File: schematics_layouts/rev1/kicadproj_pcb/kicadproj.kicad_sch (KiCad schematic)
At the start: 16 parts, among them J1 DS3231_board, J2 LM386_board, J3 microSD_board, Q1 Si2323DS_on_TO220, Q2 Si2323DS_on_TO220, SW1 WAKE Switch, SW2 SET 15MIN, U2 ATmega328P-PU

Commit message: Updated PCB layout
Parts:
- BT1, C2, C4: footprint (none) -> Connector_PinHeader_2.54mm:PinHeader_1x02_P2.54mm_Vertical
- C1, C3, C5, Q1, Q2, SW1, SW2: footprint (none) -> Connector_PinHeader_2.54mm:PinHeader_1x03_P2.54mm_Vertical
- J1, J3: footprint (none) -> Connector_PinHeader_2.54mm:PinHeader_1x06_P2.54mm_Vertical
- J2, R1, R2: footprint (none) -> Connector_PinHeader_2.54mm:PinHeader_1x04_P2.54mm_Vertical
- U2: footprint (none) -> Package_DIP:DIP-28_W7.62mm
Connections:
- net GND: now also C1.3, C3.3, C5.3, SW1.3 (2); no longer C1.2, C3.2, C5.2, SW1.2
- net at U2.1 (Pin_1): now also R1.4; no longer R1.2
- new net: R2.4, SW2.3 (2), U2.5 (Pin_5)
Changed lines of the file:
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@@
 			)
 		)
-		(property "Footprint" ""
+		(property "Footprint" "Connector_PinHeader_2.54mm:PinHeader_1x04_P2.54mm_Vertical"
 			(at 176.53 85.09 0)
 			(effects
@@
 			)
 		)
-		(property "Footprint" ""
+		(property "Footprint" "Package_DIP:DIP-28_W7.62mm"
 			(at 133.35 86.36 0)
 			(effects
@@
 	)
 	(symbol
+		(lib_name "R_1")
 		(lib_id "Device:R")
 		(at 119.38 71.12 90)
@@
 			)
 		)
-		(property "Footprint" ""
+		(property "Footprint" "Connector_PinHeader_2.54mm:PinHeader_1x04_P2.54mm_Vertical"
 			(at 119.38 72.898 90)
 			(effects
@@
 		(pin "1"
 		)
-		(pin "2"
+		(pin "4"
 		)
 		(instances
@@
 			)
 		)
-		(property "Footprint" ""
+		(property "Footprint" "Connector_PinHeader_2.54mm:PinHeader_1x02_P2.54mm_Vertical"
 			(at 153.3652 99.06 0)
 			(effects
@@
 			)
 		)
-		(property "Footprint" ""
+		(property "Footprint" "Connector_PinHeader_2.54mm:PinHeader_1x03_P2.54mm_Vertical"
 			(at 176.53 49.53 0)
 			(effects
@@
 			)
 		)
-		(property "Footprint" ""
+		(property "Footprint" "Connector_PinHeader_2.54mm:PinHeader_1x03_P2.54mm_Vertical"
 			(at 75.8952 104.14 0)
 			(effects
@@
 		(pin "1"
 		)
-		(pin "2"
+		(pin "3"
 		)
 		(instances
@@
 			)
 		)
-		(property "Footprint" ""
+		(property "Footprint" "Connector_PinHeader_2.54mm:PinHeader_1x06_P2.54mm_Vertical"
 			(at 176.53 67.31 0)
 			(effects
@@
 	)
 	(symbol
+		(lib_name "C_2")
 		(lib_id "Device:C")
 		(at 87.63 74.93 0)
@@
 			)
 		)
-		(property "Footprint" ""
+		(property "Footprint" "Connector_PinHeader_2.54mm:PinHeader_1x03_P2.54mm_Vertical"
 			(at 88.5952 78.74 0)
 			(effects
@@
 		(pin "1"
 		)
-		(pin "2"
+		(pin "3"
 		)
 		(instances
@@
 	)
 	(symbol
+		(lib_name "C_1")
 		(lib_id "Device:C")
 		(at 80.01 74.93 0)
@@
 			)
 		)
-		(property "Footprint" ""
+		(property "Footprint" "Connector_PinHeader_2.54mm:PinHeader_1x02_P2.54mm_Vertical"
 			(at 79.0448 78.74 0)
 			(effects
@@
 			)
 		)
-		(property "Footprint" ""
+		(property "Footprint" "Connector_PinHeader_2.54mm:PinHeader_1x06_P2.54mm_Vertical"
 			(at 176.53 102.87 0)
 			(effects
@@
 			)
 		)
-		(property "Footprint" ""
+		(property "Footprint" "Connector_PinHeader_2.54mm:PinHeader_1x02_P2.54mm_Vertical"
 			(at 113.03 52.07 0)
 			(effects
@@
 			)
 		)
-		(property "Footprint" ""
+		(property "Footprint" "Connector_PinHeader_2.54mm:PinHeader_1x03_P2.54mm_Vertical"
 			(at 113.03 43.18 0)
 			(effects
@@
 			)
 		)
-		(property "Footprint" ""
+		(property "Footprint" "Connector_PinHeader_2.54mm:PinHeader_1x04_P2.54mm_Vertical"
 			(at 105.41 83.058 90)
 			(effects
@@
 		(pin "1"
 		)
-		(pin "2"
+		(pin "4"
 		)
 		(instances
@@
 			)
 		)
-		(property "Footprint" ""
+		(property "Footprint" "Connector_PinHeader_2.54mm:PinHeader_1x03_P2.54mm_Vertical"
 			(at 107.95 90.17 0)
 			(effects
@@
 			)
 		)
-		(pin "2"
+		(pin "3"
 		)
 		(pin "1"
@@
 	)
 	(symbol
+		(lib_name "SW_Push_1")
 		(lib_id "Switch:SW_Push")
 		(at 146.05 40.64 0)
@@
 			)
 		)
-		(property "Footprint" ""
+		(property "Footprint" "Connector_PinHeader_2.54mm:PinHeader_1x03_P2.54mm_Vertical"
 			(at 146.05 35.56 0)
 			(effects
@@
 			)
 		)
-		(pin "2"
+		(pin "3"
 		)
 		(pin "1"
@@
 	)
 	(symbol
+		(lib_name "CP_1")
 		(lib_id "Device:CP")
 		(at 199.39 86.36 0)
@@
 			)
 		)
-		(property "Footprint" ""
+		(property "Footprint" "Connector_PinHeader_2.54mm:PinHeader_1x03_P2.54mm_Vertical"
 			(at 200.3552 90.17 0)
 			(effects
@@
 			)
 		)
-		(pin "2"
-		)
-		(pin "1"
+		(pin "3"
+		)
+		(pin "1"

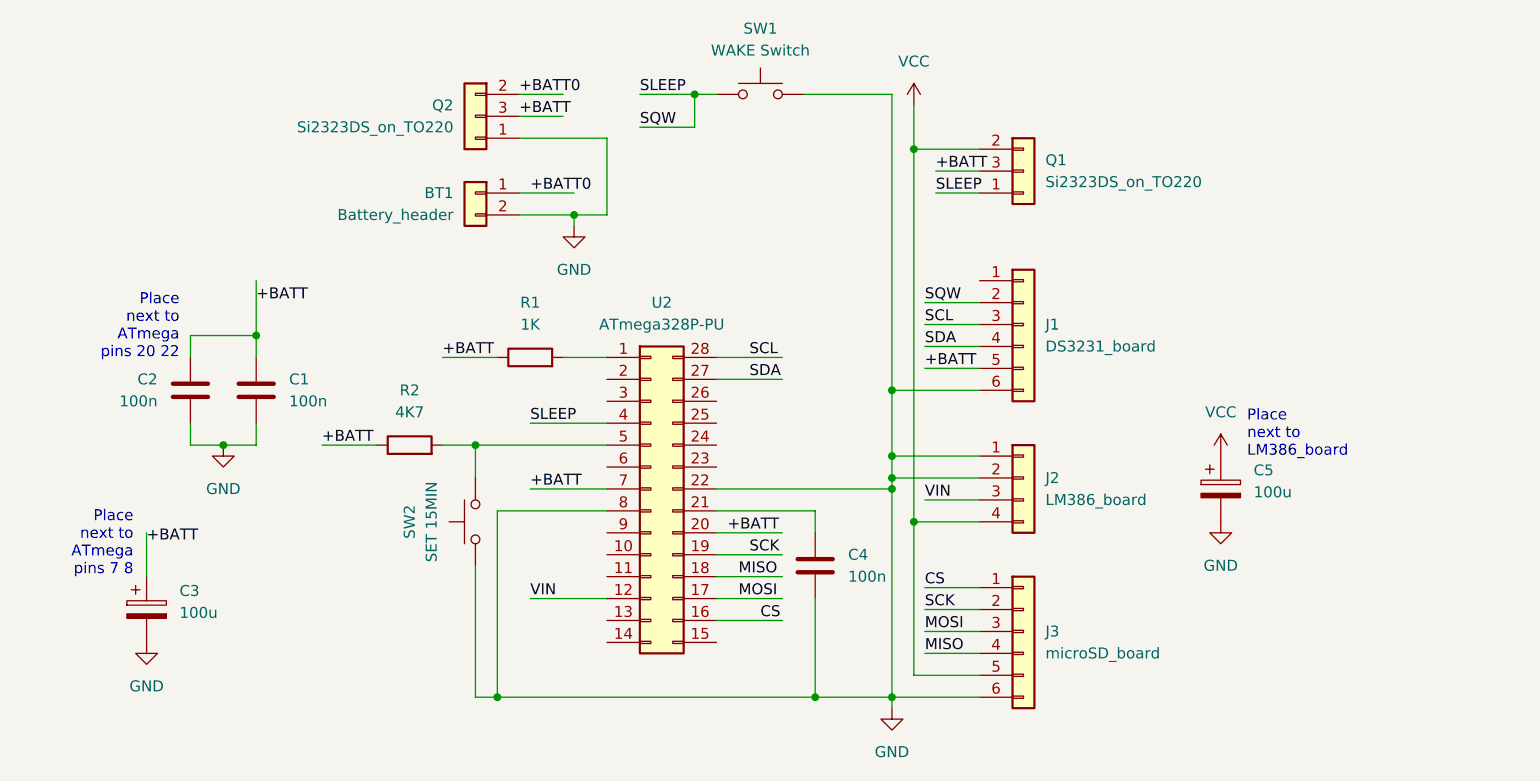
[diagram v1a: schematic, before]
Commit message: Revised PCB layout; Updated documentation
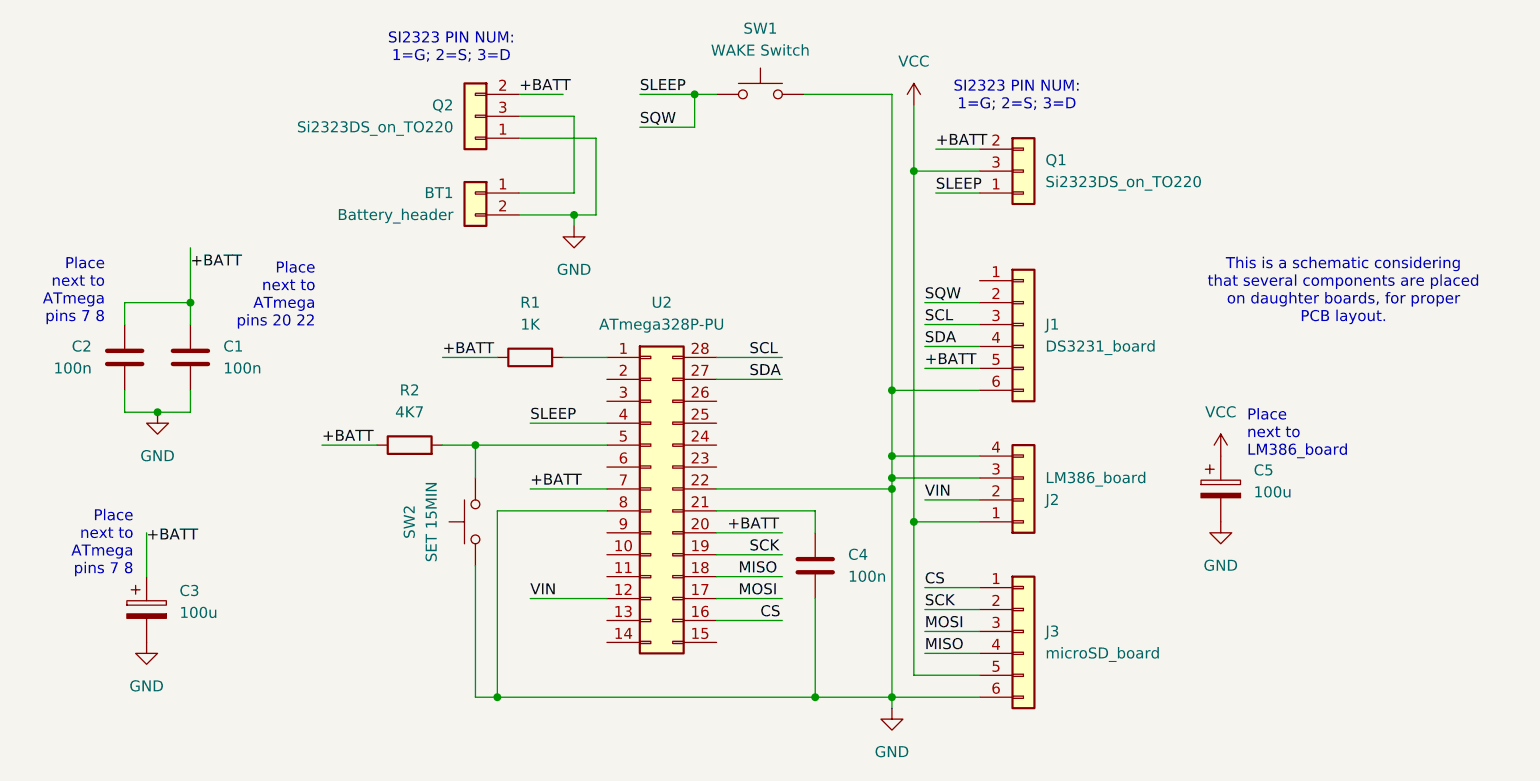
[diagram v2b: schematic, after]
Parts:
- C3: footprint Connector_PinHeader_2.54mm:PinHeader_1x03_P2.54mm_Vertical -> Connector_PinHeader_2.54mm:PinHeader_1x02_P2.54mm_Vertical
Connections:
- net +BATT: now also Q1.2 (Pin_1), Q2.2 (Pin_1); no longer Q1.3 (Pin_2), Q2.3 (Pin_2)
- net GND: now also C3.2, J2.3 (Pin_3), J2.4 (Pin_4), SW2.3 (2); no longer C3.3, J2.1 (Pin_1), J2.2 (Pin_2), SW2.1
- net VCC: now also J2.1 (Pin_1), Q1.3 (Pin_2); no longer J2.4 (Pin_4), Q1.2 (Pin_1)
- net VIN: now also J2.2 (Pin_2); no longer J2.3 (Pin_3)
- net at R2.4, U2.5 (Pin_5): now also SW2.1; no longer SW2.3 (2)
- net +BATT0: no longer names the net of BT1.1 (Pin_1)
- net +BATT0: now also Q2.3 (Pin_2); no longer Q2.2 (Pin_1)
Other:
- note added: "SI2323 PIN NUM: 1=G; 2=S; 3=D"
- note added: "This is a schematic considering that several components are placed on daughter boards, for proper PCB layout."
- title: (none) -> Seikosha80 Westminster Chimer
- moved on the sheet: C1, C2

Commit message: Revised all docs, removed C5 (never heard about it); Updated wiki with some news
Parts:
- removed C5: 100u, Connector_PinHeader_2.54mm:PinHeader_1x03_P2.54mm_Vertical, symbol Device:CP
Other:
- note removed: "Place next to LM386_board"
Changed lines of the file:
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@@
-		)
-	)
-	(text "Place\nnext to\nLM386_board"
-		(exclude_from_sim no)
-		(at 202.438 80.01 0)
-		(effects
-			(font
-				(size 1.27 1.27)
-			)
-			(justify left)
 		)
 	)
@@
 				(path "/3b7fe0ff-041d-4733-b3a1-7b46657d152e"
 					(reference "J2")
-					(unit 1)
-				)
-			)
-		)
-	)
-	(symbol
-		(lib_id "power:VCC")
-		(at 199.39 82.55 0)
-		(unit 1)
-		(exclude_from_sim no)
-		(in_bom yes)
-		(on_board yes)
-		(dnp no)
-		(fields_autoplaced yes)
-		(property "Reference" "#PWR03"
-			(at 199.39 86.36 0)
-			(effects
-				(font
-					(size 1.27 1.27)
-				)
-				(hide yes)
-			)
-		)
-		(property "Value" "VCC"
-			(at 199.39 77.47 0)
-			(effects
-				(font
-					(size 1.27 1.27)
-				)
-			)
-		)
-		(property "Footprint" ""
-			(at 199.39 82.55 0)
-			(effects
-				(font
-					(size 1.27 1.27)
-				)
-				(hide yes)
-			)
-		)
-		(property "Datasheet" ""
-			(at 199.39 82.55 0)
-			(effects
-				(font
-					(size 1.27 1.27)
-				)
-				(hide yes)
-			)
-		)
-		(property "Description" "Power symbol creates a global label with name \"VCC\""
-			(at 199.39 82.55 0)
-			(effects
-				(font
-					(size 1.27 1.27)
-				)
-				(hide yes)
-			)
-		)
-		(pin "1"
-		)
-		(instances
-			(project "kicadproj"
-				(path "/3b7fe0ff-041d-4733-b3a1-7b46657d152e"
-					(reference "#PWR03")
 					(unit 1)
 				)
@@
 	)
 	(symbol
-		(lib_id "power:GND")
-		(at 199.39 90.17 0)
-		(unit 1)
-		(exclude_from_sim no)
-		(in_bom yes)
-		(on_board yes)
-		(dnp no)
-		(fields_autoplaced yes)
-		(property "Reference" "#PWR05"
-			(at 199.39 96.52 0)
-			(effects
-				(font
-					(size 1.27 1.27)
-				)
-				(hide yes)
-			)
-		)
-		(property "Value" "GND"
-			(at 199.39 95.25 0)
-			(effects
-				(font
-					(size 1.27 1.27)
-				)
-			)
-		)
-		(property "Footprint" ""
-			(at 199.39 90.17 0)
-			(effects
-				(font
-					(size 1.27 1.27)
-				)
-				(hide yes)
-			)
-		)
-		(property "Datasheet" ""
-			(at 199.39 90.17 0)
-			(effects
-				(font
-					(size 1.27 1.27)
-				)
-				(hide yes)
-			)
-		)
-		(property "Description" "Power symbol creates a global label with name \"GND\" , ground"
-			(at 199.39 90.17 0)
-			(effects
-				(font
-					(size 1.27 1.27)
-				)
-				(hide yes)
-			)
-		)
-		(pin "1"
-		)
-		(instances
-			(project "kicadproj"
-				(path "/3b7fe0ff-041d-4733-b3a1-7b46657d152e"
-					(reference "#PWR05")
-					(unit 1)
-				)
-			)
-		)
-	)
-	(symbol
 		(lib_id "Switch:SW_Push")
 		(at 113.03 90.17 90)
@@
 					(unit 1)
 				)
-			)
-		)
-	)
-	(symbol
-		(lib_name "CP_1")
-		(lib_id "Device:CP")
-		(at 199.39 86.36 0)
-		(unit 1)
-		(exclude_from_sim no)
-		(in_bom yes)
-		(on_board yes)
-		(dnp no)
-		(fields_autoplaced yes)
-		(property "Reference" "C5"
-			(at 203.2 84.2009 0)
-			(effects
-				(font
-					(size 1.27 1.27)
-				)
-				(justify left)
-			)
-		)
-		(property "Value" "100u"
-			(at 203.2 86.7409 0)
-			(effects
-				(font
-					(size 1.27 1.27)
-				)
-				(justify left)
-			)
-		)
-		(property "Footprint" "Connector_PinHeader_2.54mm:PinHeader_1x03_P2.54mm_Vertical"
-			(at 200.3552 90.17 0)
-			(effects
-				(font
-					(size 1.27 1.27)
-				)
-				(hide yes)
-			)
-		)
-		(property "Datasheet" "~"
-			(at 199.39 86.36 0)
-			(effects
-				(font
-					(size 1.27 1.27)
-				)
-				(hide yes)
-			)
-		)
-		(property "Description" "Polarized capacitor"
-			(at 199.39 86.36 0)
-			(effects
-				(font
-					(size 1.27 1.27)
-				)
-				(hide yes)
-			)
-		)
-		(pin "3"
-		)
-		(pin "1"
-		)
-		(instances
-			(project "kicadproj"
-				(path "/3b7fe0ff-041d-4733-b3a1-7b46657d152e"
-					(reference "C5")
-					(unit 1)
-				)
